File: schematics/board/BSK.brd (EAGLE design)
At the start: 94 x 94 mm, 56 parts

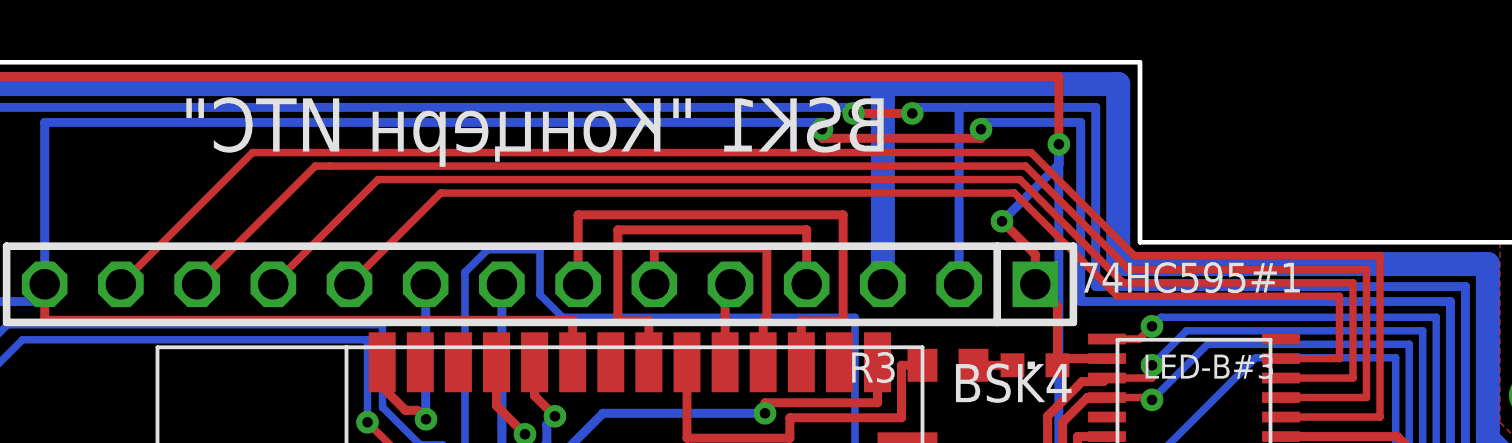
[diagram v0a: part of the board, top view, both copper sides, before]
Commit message: Подписаны разъемы на платах
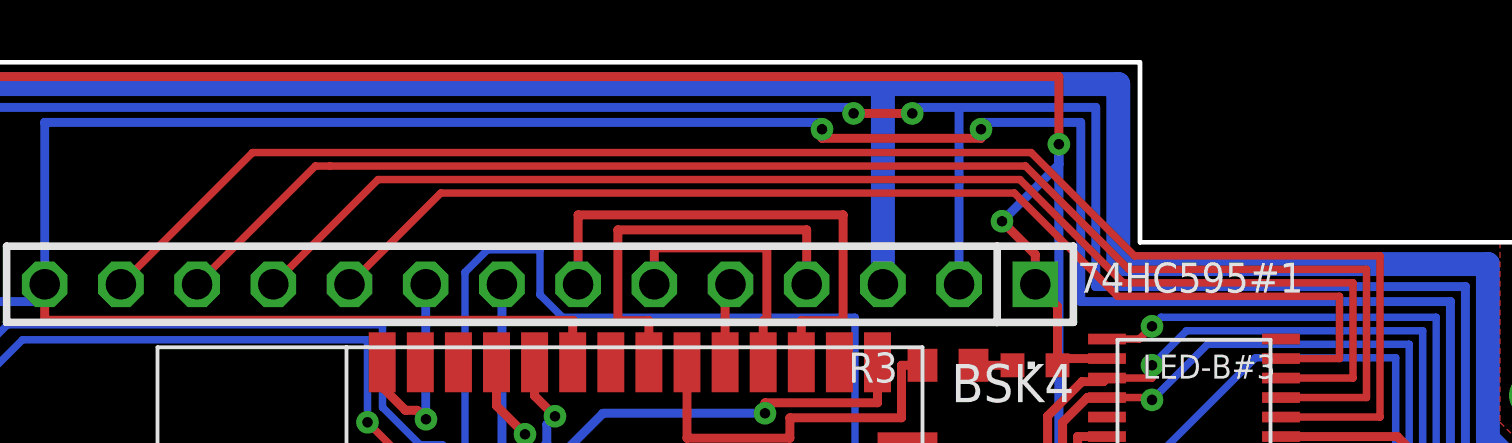
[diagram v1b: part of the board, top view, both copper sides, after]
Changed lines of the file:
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@@
 <text x="36.96" y="69.51" size="1" layer="25" rot="R90" align="center">BUS</text>
 <text x="69.02" y="61.59" size="1" layer="25" rot="R90" align="center">EM</text>
-<text x="35" y="92.8" size="1.778" layer="25" rot="MR180">BSK1 "Концерн ИТС"</text>
 <circle x="47" y="47" radius="15.25" width="0.2" layer="20"/>
 </plain>

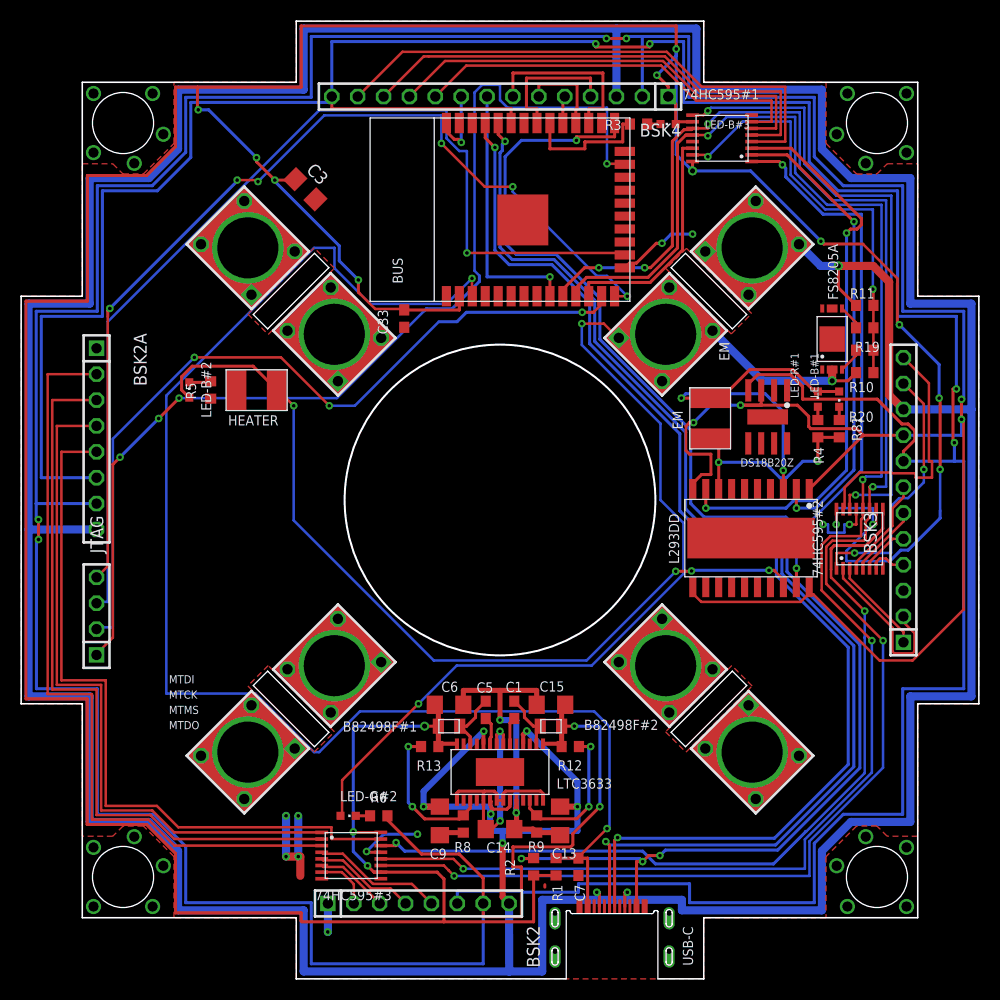
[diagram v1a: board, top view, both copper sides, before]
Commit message: Внёс незначительные правки на платах. Но пока не везде
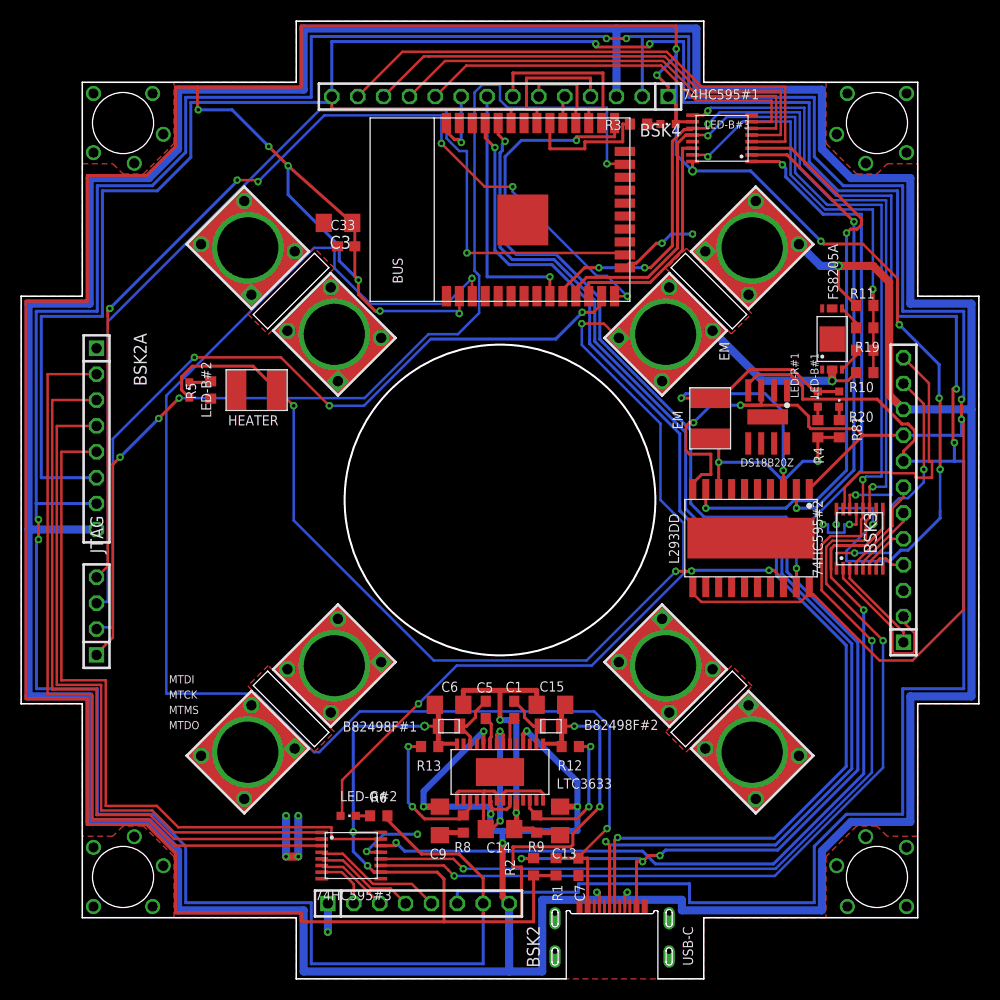
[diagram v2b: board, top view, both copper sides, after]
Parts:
- moved C33 9.10 mm to (31.9, 71.9), turned to 180 degrees
- moved C3 4.60 mm to (31.1, 74.2), turned to 180 degrees
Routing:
- net VDD: track 392.2 -> 406.4 mm, vias 16 -> 18
- net GND: track 76.8 -> 74.5 mm
- net SHCP: track 172.0 -> 170.0 mm
- net MTDO: track 103.9 -> 105.7 mm
- net STCP: track 167.7 -> 166.0 mm

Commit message: Исправлены компоненты
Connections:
- net GND: no longer U$13.32
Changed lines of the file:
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@@
 <?xml version="1.0" encoding="utf-8"?>
 <!DOCTYPE eagle SYSTEM "eagle.dtd">
-<eagle version="9.5.1">
+<eagle version="9.6.0">
 <drawing>
 <settings>
@@
 <wire x1="27" y1="0" x2="53.5" y2="0" width="0.1524" layer="20"/>
 <wire x1="67" y1="0" x2="62.5" y2="0" width="0.1524" layer="20"/>
-<text x="14.5" y="29" size="0.8" layer="25">MTDI</text>
-<text x="14.5" y="27.5" size="0.8" layer="25">MTCK</text>
-<text x="14.5" y="26" size="0.8" layer="25">MTMS</text>
-<text x="14.5" y="24.5" size="0.8" layer="25">MTDO</text>
+<text x="9.9" y="37.3" size="0.8" layer="25">MTDI</text>
+<text x="9.9" y="35.8" size="0.8" layer="25">MTCK</text>
+<text x="9.9" y="34.3" size="0.8" layer="25">MTMS</text>
+<text x="9.9" y="32.8" size="0.8" layer="25">MTDO</text>
 <text x="39" y="2" size="1.5" layer="26" rot="MR0" align="center">to BSK2</text>
 <text x="92" y="47" size="1.5" layer="26" rot="SMR270" align="center">to BSK3</text>
@@
 <contactref element="C15" pad="2"/>
 <contactref element="C13" pad="2"/>
-<contactref element="U$13" pad="1" route="any" routetag="G$1.GND"/>
-<contactref element="U$13" pad="15" route="any" routetag="G$1.GND"/>
-<contactref element="U$13" pad="38" route="any" routetag="G$1.GND"/>
-<contactref element="U$13" pad="32" route="any" routetag="G$1.GND"/>
+<contactref element="U$13" pad="1"/>
+<contactref element="U$13" pad="15"/>
+<contactref element="U$13" pad="38"/>
 <contactref element="74HC595#1" pad="8"/>
 <contactref element="74HC595#2" pad="8"/>

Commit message: Платы подготовлены для Резонита
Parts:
- moved R3 2.34 mm to (62.1, 82.1)
- moved LED-B#3 1.41 mm to (62.1, 83.7)
- moved LED-R#1 1.26 mm to (79.4, 56.5)
- moved R4 1.26 mm to (79.4, 53.6)
- moved R81 1.26 mm to (81.5, 53.6)
- moved LED-B#1 1.26 mm to (81.5, 56.5)
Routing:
- net 5V: track 438.1 -> 440.0 mm
- net VDD: track 406.4 -> 408.0 mm
- net N$1: track 36.1 -> 37.4 mm
- net N$2: track 20.8 -> 21.8 mm
- net N$34: track 1.30 -> 2.26 mm
- net 1W: track 322.3 -> 321.6 mm
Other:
- board text added: "EM+"
- board text added: "EM-"
- board text added: "HEATER"
- board text added: "IO1"
- board text removed: "EM"

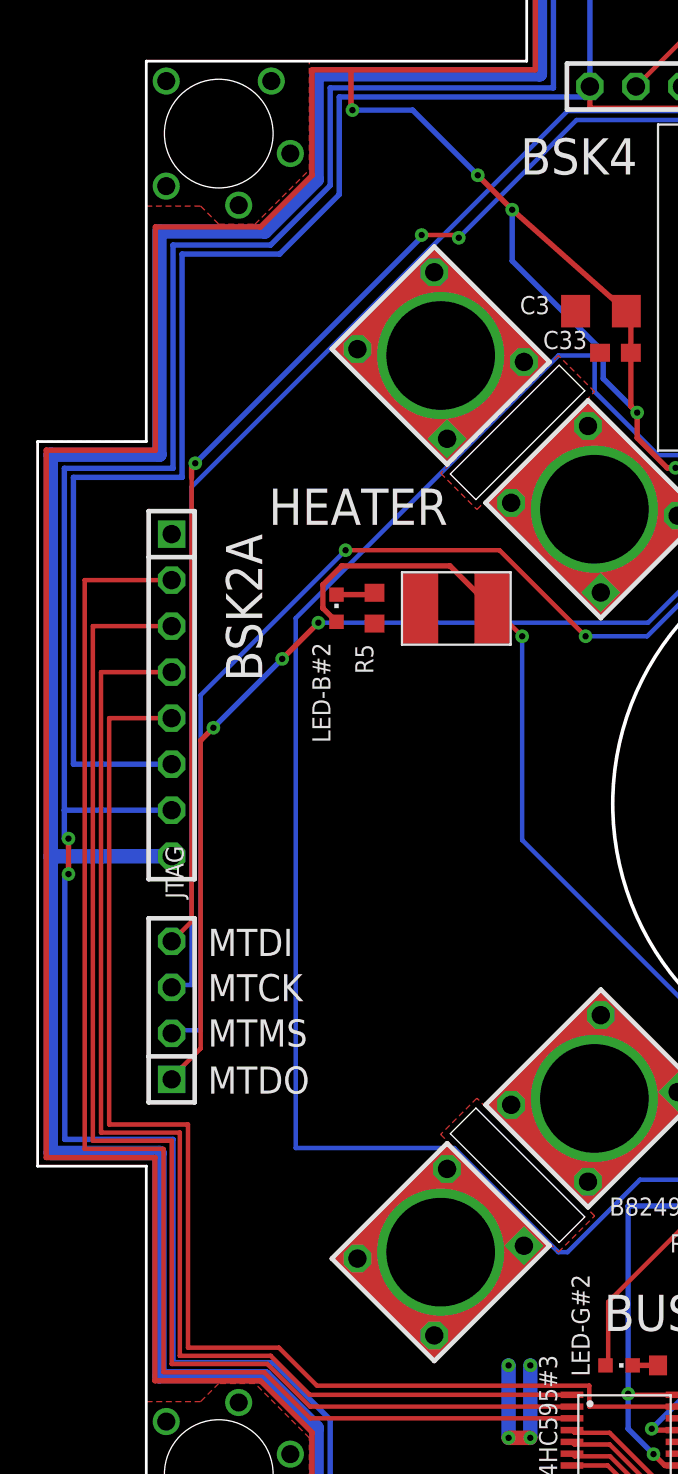
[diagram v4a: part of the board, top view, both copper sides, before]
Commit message: Исправлены АРК и БСК1
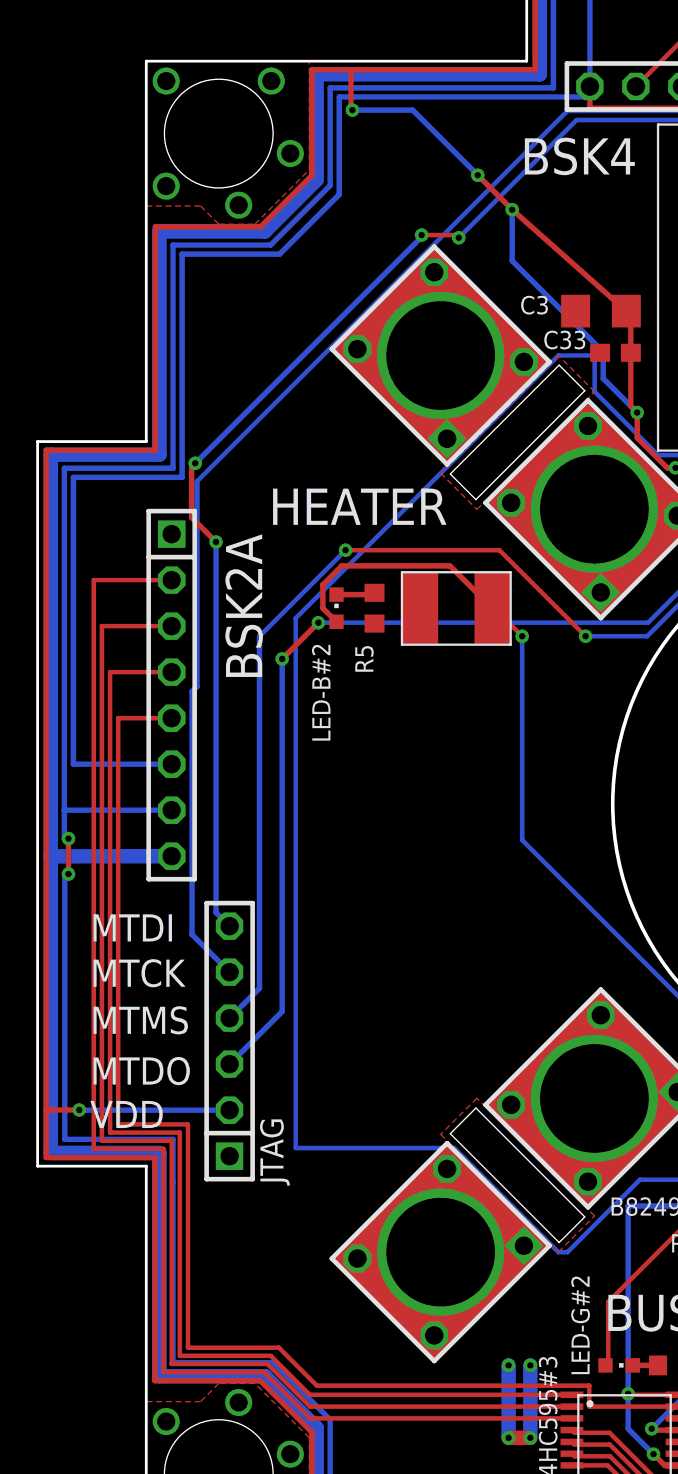
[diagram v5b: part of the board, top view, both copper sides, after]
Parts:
- JTAG: device pinheadCS:1X04 -> pinheadCS:1X06
- moved JTAG 3.62 mm to (10.6, 33.9)
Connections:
- net GND: now also JTAG.1
- net MTCK: now also JTAG.5; no longer JTAG.3
- net MTDI: now also JTAG.6; no longer JTAG.4
- net MTDO: now also JTAG.3; no longer JTAG.1
- net MTMS: now also JTAG.4; no longer JTAG.2
- net VDD: now also JTAG.2
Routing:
- net VDD: track 408.0 -> 418.1 mm, vias 18 -> 19
- net MTMS: track 78.5 -> 75.5 mm
- net MTDO: track 105.7 -> 103.6 mm, vias 4 -> 3
- net MTCK: track 101.5 -> 100.4 mm
- net B2A_KVCC: track 71.6 -> 70.6 mm
- net B2A_KHEAT: track 68.5 -> 67.5 mm
- net B2A_KEM-: track 76.5 -> 75.5 mm
- net B2A_KEM+: track 72.5 -> 71.5 mm
- net MTDI: track 96.3 -> 95.8 mm, vias 6 -> 7
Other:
- board text added: "VDD"

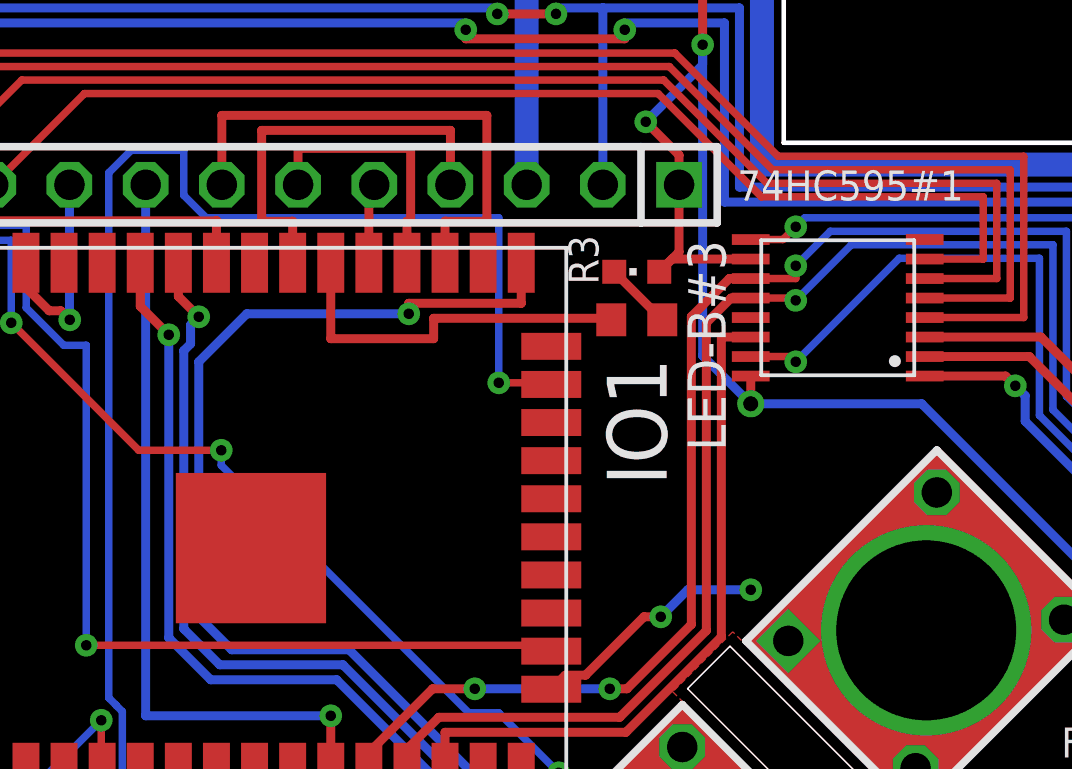
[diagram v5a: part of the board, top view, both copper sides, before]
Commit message: Добавлены подтяжки i2c
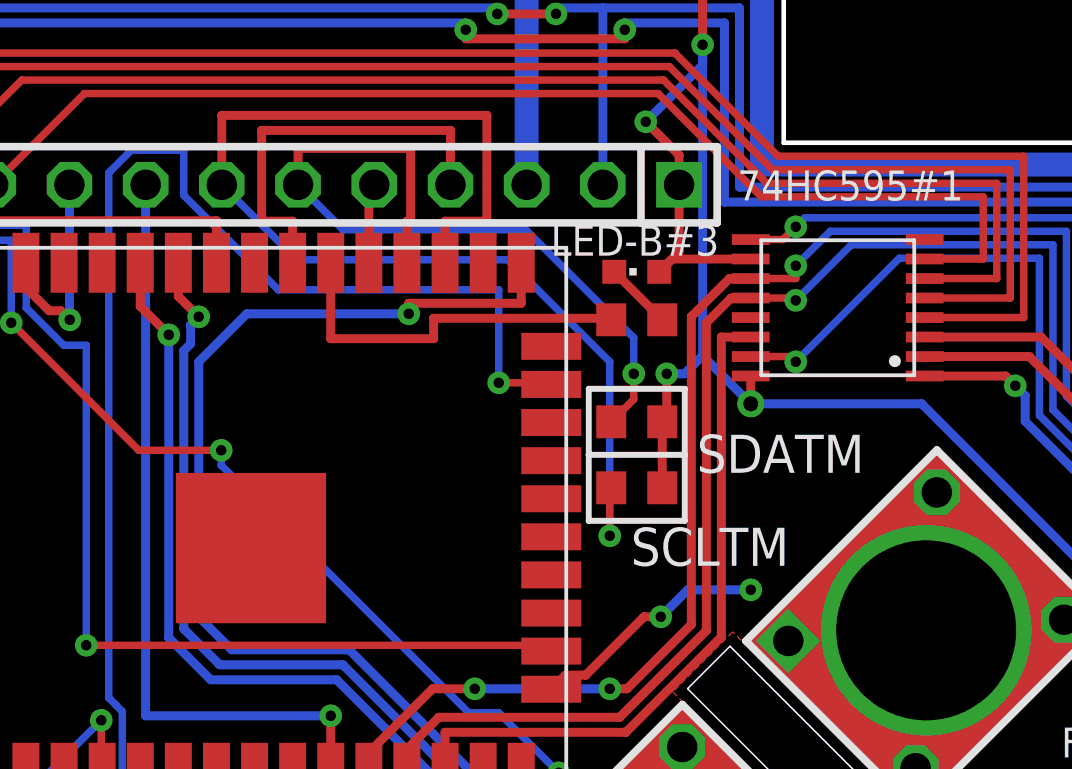
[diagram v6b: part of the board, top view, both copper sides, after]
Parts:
- added R14, R7: 5k1, resistor:R0603
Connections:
- net SCLTM: now also R7.2
- net SDATM: now also R14.2
- net VDD: now also R14.1, R7.1
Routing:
- net SCLTM: track 17.5 -> 40.2 mm, vias 0 -> 1
- net SDATM: track 8.90 -> 25.3 mm, vias 0 -> 1
- net VDD: track 418.1 -> 423.5 mm, vias 19 -> 20
- net MTDO: track 103.6 -> 102.2 mm
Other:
- board text added: "SCLTM"
- board text added: "SDATM"
- board text removed: "IO1"
